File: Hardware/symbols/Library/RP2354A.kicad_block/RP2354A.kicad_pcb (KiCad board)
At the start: 4 copper layers, 20 x 29 mm, 30 parts, among them U1 RP2354A, Y1 ABM8-272-T3

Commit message: Turn the rp2354a reference design into a design block
This removes the BM28 connector, since the expectation is that we can
now just place the design directly onto a board rather than connecting a
helper board.  It also removes some other random details that made sense
as a discrete board (like the power and GPIO LEDs but also the BOOTSEL
switch) but should would be done by the board that uses this design
block.

This also is much more aggressive about using smaller components, just
to make it possibly to route out all the GPIOs.  The original design
didn't route out everything because the end result was still limited by
the BM28 connector (and my expectation of not needing so many GPIOs),
and avoided 0201 components.

The 10uF bulk bypass capacitors have also been BOM-consolidated to
4.7uF: they came from the RP2350 minimal design, but they were actually
centered around the 3.3V LDO.  I'm keeping them around in the smaller
form, feeding the 100nF bypass capacitors.

Hopefully the end result works - both as a design block and as hardware
design.  We will find out.

Signed-off-by: Linus Torvalds <torvalds@linux-foundation.org>
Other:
- board outline removed

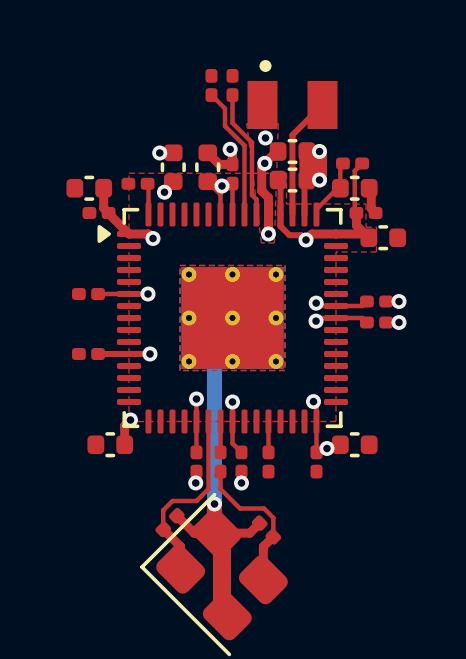
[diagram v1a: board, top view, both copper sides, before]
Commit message: Avoid using zones in the RP2354A design block
Using zones in design blocks doesn't seem to work very well in practice,
at least in the version I have (10.0.4).

I'm not entirely sure what is going on, but what seems to happen is that
when a design block is imported into a PCB design (with the "update pcb
from schematic" workflow), kicad will import it as a group, but then try
to merge matching zones with the outside.  And really confuse the
grouping as a result, and also end up mixing up the zones occasionally
so that the zone names are just completely wrong and misleading.

Sometimes it gets so bad that you end up with zones that you can see on
the PCB, but not actually access from the UI.  No way to delete the
stale zombie left-overs.  At one point I ended up rescuing one PCB by
editing the kicad_pcb file by hand and removing a group that seemed to
only exist as a grouping of zombie zones that no longer existed in
reality.

NOTE! The above is purely a symptom description from what I've seen, not
any kind of deeper understanding of what kicad actually does.  There
might be something entirely else going on, and I'm just confused.

Whatever the real issue is, zones _work_, but they seem to have a
propensity for causing problems, and I've never seen it with normal
elements.  The TAC5242 design never caused me any problems - it doesn't
use any zones (except for the base ground plane that isn't part of the
design block export).

Anyway, I can just route the power rails under the RP2354 manually using
actual traces.  It's not like it's even all that complicated: the zones
were there just to tie the room together.

Let's see if this gets rid of some of the oddities of using pre-routed
design blocks.

Signed-off-by: Linus Torvalds <torvalds@linux-foundation.org>
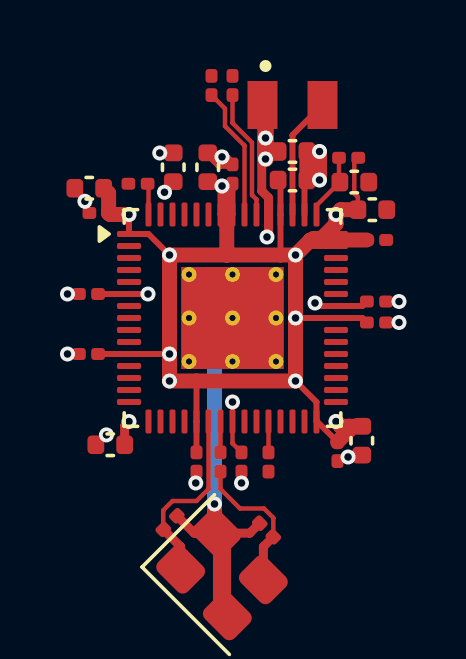
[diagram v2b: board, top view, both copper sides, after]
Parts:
- moved C21 1.00 mm to (104.7, 96.4)
- moved C14 0.97 mm to (104.8, 97.4)
- moved C13 0.78 mm to (103.5, 104.5)
- moved C19 0.27 mm to (104.3, 104.1), turned to -90 degrees
- moved R1 0.23 mm to (103.9, 94.7)
- moved C5 0.21 mm to (104.1, 95.5)
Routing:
- net +3V3: track 24.8 -> 71.4 mm, vias 9 -> 11
- net +1V1: track 12.6 -> 30.4 mm
- net GND: track 19.0 -> 18.0 mm, vias 9 -> 14
- removed copper zone on F.Cu, net +1V1
- removed copper zone on In2.Cu, net +1V1
- removed copper zone on F.Cu, net +3V3
- removed copper zone on In1.Cu, net +3V3
- removed copper zone on B.Cu, net GND
- removed copper zone on F.Cu, net GND
- removed copper zone on In1.Cu, net GND
- removed copper zone on In2.Cu, net GND
